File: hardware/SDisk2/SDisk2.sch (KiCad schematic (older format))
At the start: 34 parts

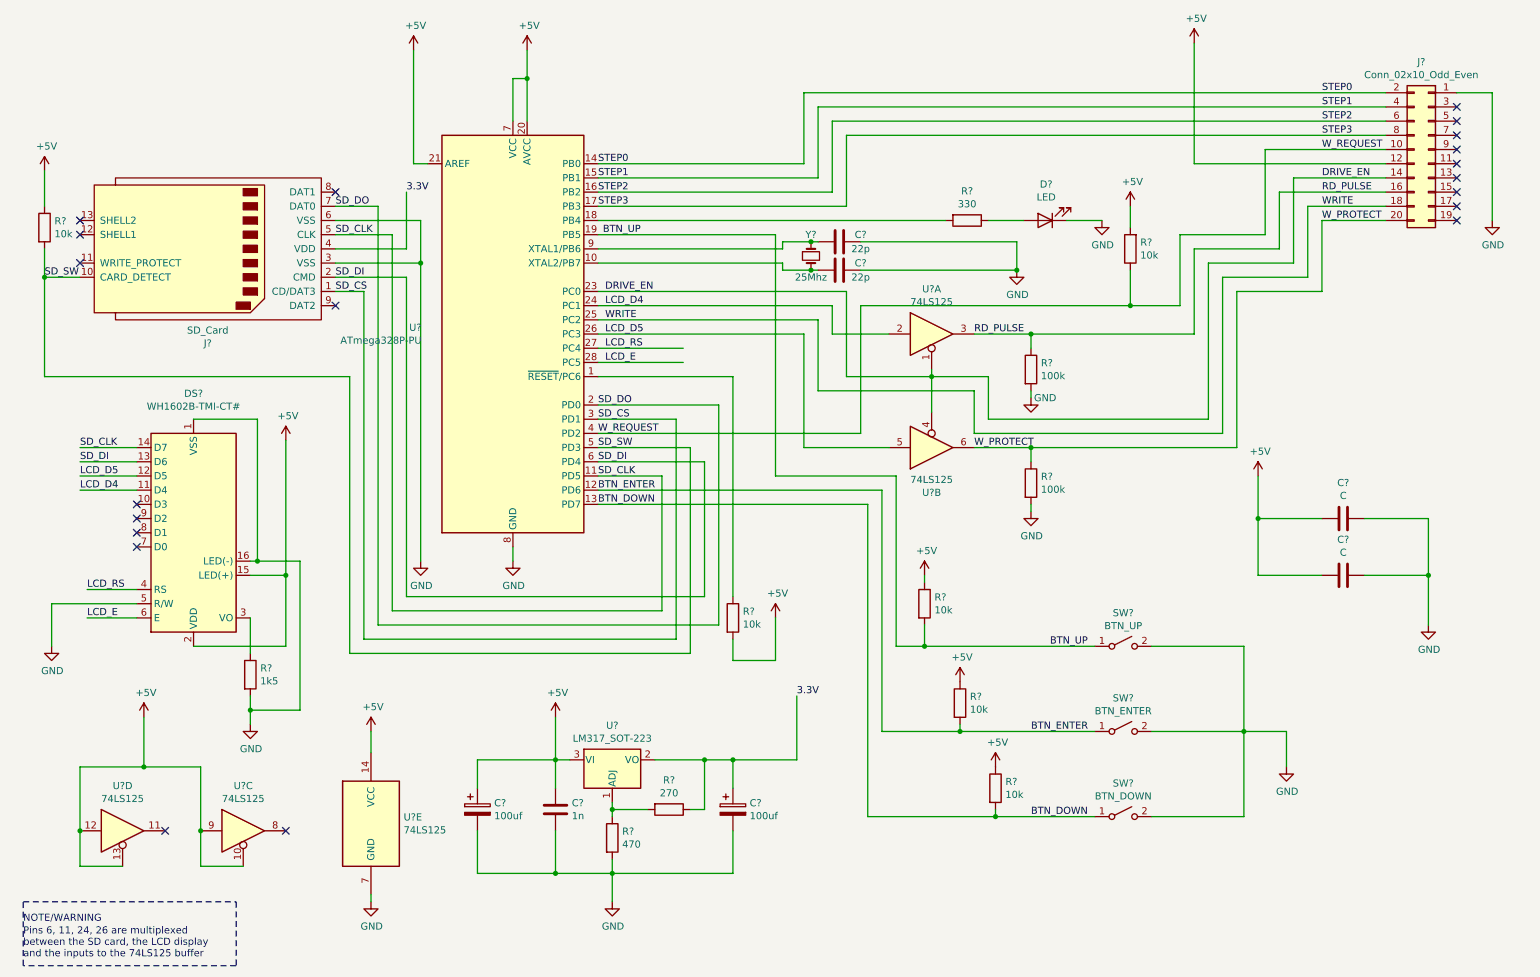
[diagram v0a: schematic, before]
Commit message: Associate footprints for most of the components
Need to create footprints for sdcard holder and LCD display

Signed-off-by: Rangel Ivanov <rangelivanov88@gmail.com>
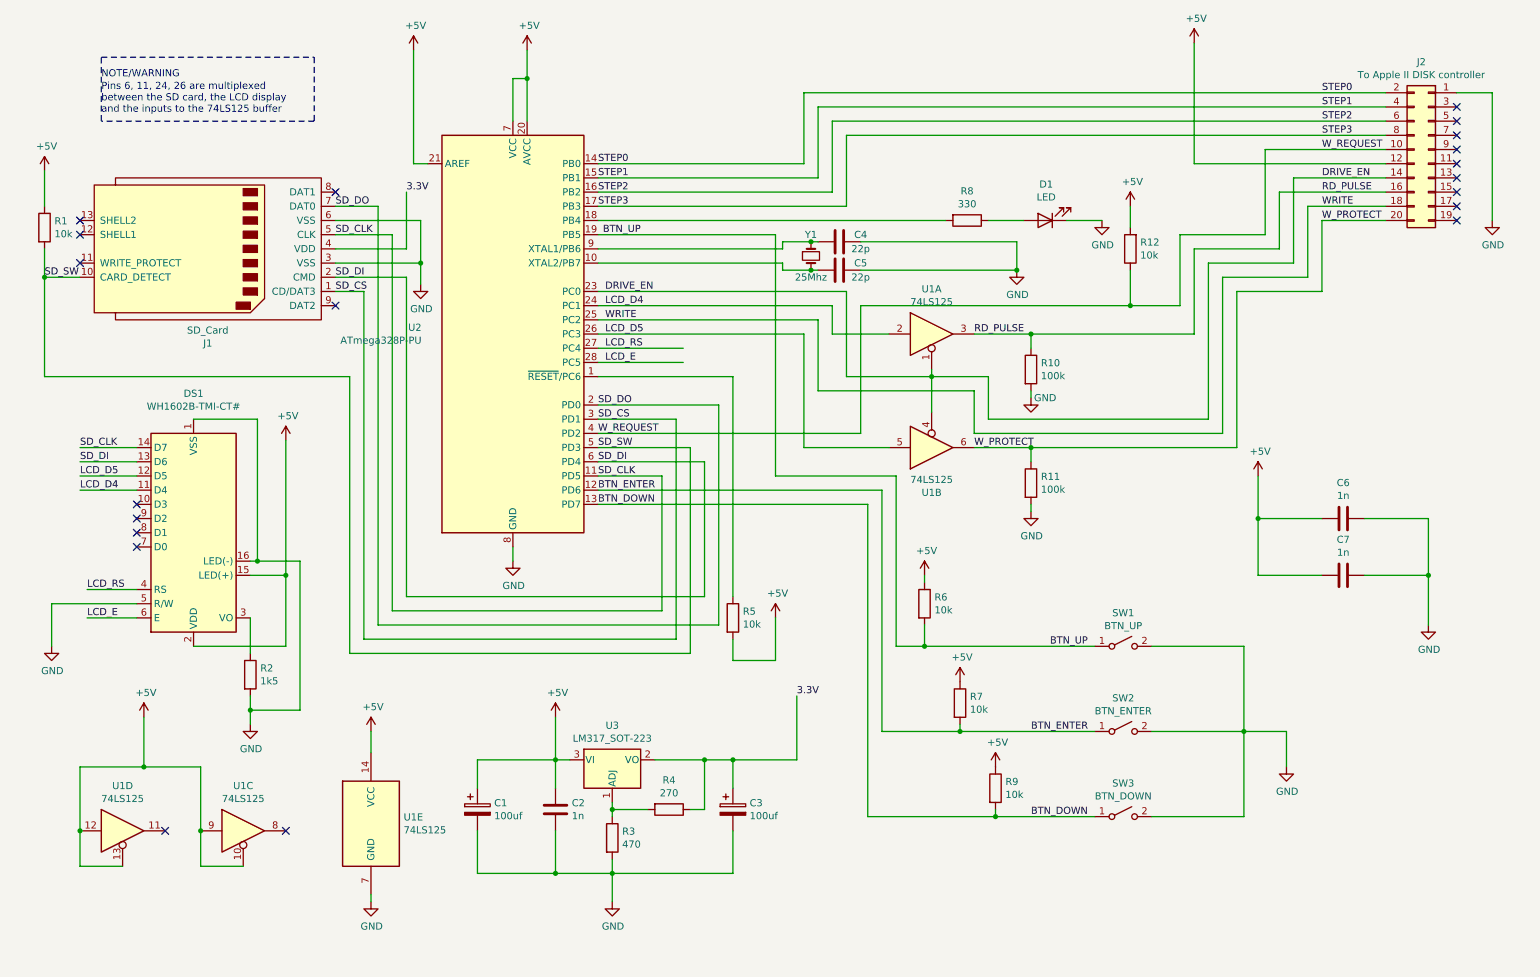
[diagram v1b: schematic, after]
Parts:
- C1, C3: renamed from C?; footprint (none) -> Capacitor_THT:CP_Radial_D5.0mm_P2.00mm
- C2, C4, C5: renamed from C?; footprint (none) -> Capacitor_THT:C_Disc_D3.0mm_W1.6mm_P2.50mm
- C6, C7: renamed from C?; value C -> 1n; footprint (none) -> Capacitor_THT:C_Disc_D3.0mm_W1.6mm_P2.50mm
- D1: renamed from D?; footprint (none) -> LED_THT:LED_D3.0mm
- DS1: renamed from DS?; footprint Display:WC1602A -> (none)
- J2: renamed from J?; value Conn_02x10_Odd_Even -> To Apple II DISK controller; footprint (none) -> Connector_PinHeader_2.54mm:PinHeader_2x10_P2.54mm_Horizontal
- R1, R10, R11, R12, R2, R3, R5, R6, R7, R8, R9: renamed from R?; footprint (none) -> Resistor_THT:R_Axial_DIN0204_L3.6mm_D1.6mm_P5.08mm_Horizontal
- R4: renamed from R?; footprint (none) -> Resistor_THT:R_Axial_DIN0204_L3.6mm_D1.6mm_P5.08mm_Vertical
- SW1, SW2, SW3: renamed from SW?; footprint (none) -> Button_Switch_THT:SW_PUSH_6mm
- U1: renamed from U?; footprint (none) -> Package_DIP:DIP-14_W7.62mm
- U3: renamed from U?; footprint Package_TO_SOT_SMD:SOT-223-3_TabPin2 -> Package_TO_SOT_THT:TO-220-3_Vertical
- Y1: renamed from Y?; footprint (none) -> Crystal:Crystal_HC49-4H_Vertical
- gave numbers to parts that had none: 2

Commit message: Add SDCard footprint and datasheet
Signed-off-by: Rangel Ivanov <rangelivanov88@gmail.com>
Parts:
- J1: footprint (none) -> SDisk2:attend-104d-tca0-r06-sdcard-holder; symbol Connector:SD_Card -> SDisk2:SD_Card
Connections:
- net GND: now also J1.13 (GND)
- no-connect marks 20 -> 19
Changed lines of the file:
@@
 	-1   0    0    1
 $EndComp
-Wire Wire Line
-	8350 2250 8350 2100
 $Comp
 L power:+5V #PWR0110
@@
 Wire Wire Line
 	2950 2700 2750 2700
-$Comp
-L Connector:SD_Card J1
-U 1 1 5FF919EB
-P 1850 2400
-F 0 "J1" H 1850 3065 50  0000 C CNN
-F 1 "SD_Card" H 1850 2974 50  0000 C CNN
-F 2 "" H 1850 2400 50  0001 C CNN
-F 3 "http://portal.fciconnect.com/Comergent//fci/drawing/10067847.pdf" H 1850 2400 50  0001 C CNN
-	1    1850 2400
-	-1   0    0    1
-$EndComp
 Text Label 2750 2100 0    50   ~ 0
 SD_DO
@@
 Text Notes 1100 1200 0    50   ~ 0
 NOTE/WARNING\n
-NoConn ~ 950  2200
 NoConn ~ 950  2300
 Text Label 7650 6400 0    50   ~ 0
@@
 Text Label 8050 5200 2    50   ~ 0
 BTN_UP
+Wire Wire Line
+	8350 2050 8350 2100
+Connection ~ 8350 2100
+Wire Wire Line
+	8350 2100 8350 2250
+$Comp
+L SDisk2:SD_Card J1
+U 1 1 5FF919EB
+P 1850 2400
+F 0 "J1" H 1850 3065 50  0000 C CNN
+F 1 "SD_Card" H 1850 2974 50  0000 C CNN
+F 2 "SDisk2:attend-104d-tca0-r06-sdcard-holder" H 1850 2400 50  0001 C CNN
+F 3 "http://portal.fciconnect.com/Comergent//fci/drawing/10067847.pdf" H 1850 2400 50  0001 C CNN
+	1    1850 2400
+	-1   0    0    1
+$EndComp
+Wire Wire Line
+	950  2200 900  2200
+Wire Wire Line
+	900  2200 900  2950
+$Comp
+L power:GND #PWR0128
+U 1 1 5FFFE7B3
+P 900 2950
+F 0 "#PWR0128" H 900 2700 50  0001 C CNN
+F 1 "GND" H 905 2777 50  0000 C CNN
+F 2 "" H 900 2950 50  0001 C CNN
+F 3 "" H 900 2950 50  0001 C CNN
+	1    900  2950
+	1    0    0    -1
+$EndComp
 $EndSCHEMATC

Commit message: Create netlist and begin place and route
Signed-off-by: Rangel Ivanov <rangelivanov88@gmail.com>
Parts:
- DS1: footprint (none) -> Connector_PinHeader_2.54mm:PinHeader_1x16_P2.54mm_Vertical
- R4: footprint Resistor_THT:R_Axial_DIN0204_L3.6mm_D1.6mm_P5.08mm_Vertical -> Resistor_THT:R_Axial_DIN0204_L3.6mm_D1.6mm_P5.08mm_Horizontal
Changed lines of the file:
@@
 F 0 "R4" V 4893 6350 50  0000 C CNN
 F 1 "270" V 4984 6350 50  0000 C CNN
-F 2 "Resistor_THT:R_Axial_DIN0204_L3.6mm_D1.6mm_P5.08mm_Vertical" V 5030 6350 50  0001 C CNN
+F 2 "Resistor_THT:R_Axial_DIN0204_L3.6mm_D1.6mm_P5.08mm_Horizontal" V 5030 6350 50  0001 C CNN
 F 3 "~" H 5100 6350 50  0001 C CNN
 	1    5100 6350
@@
 F 0 "DS1" H 1750 3419 50  0000 C CNN
 F 1 "WH1602B-TMI-CT# " H 1750 3510 50  0000 C CNN
-F 2 "" H 1750 3500 50  0001 C CIN
+F 2 "Connector_PinHeader_2.54mm:PinHeader_1x16_P2.54mm_Vertical" H 1750 3500 50  0001 C CIN
 F 3 "https://store.comet.bg/download-file.php?id=1596" H 2450 4400 50  0001 C CNN
 	1    1750 4400
@@
 F 1 "SD_Card" H 1850 2974 50  0000 C CNN
 F 2 "SDisk2:attend-104d-tca0-r06-sdcard-holder" H 1850 2400 50  0001 C CNN
-F 3 "http://portal.fciconnect.com/Comergent//fci/drawing/10067847.pdf" H 1850 2400 50  0001 C CNN
+F 3 "https://store.comet.bg/download-file.php?id=8828" H 1850 2400 50  0001 C CNN
 	1    1850 2400
 	-1   0    0    1

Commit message: Move symbols to project specific symbol library
Signed-off-by: Rangel Ivanov <rangelivanov88@gmail.com>
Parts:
- DS1: symbol Display_Character:WC1602A -> SDisk2:WC1602B
- U1: symbol 74xx:74LS125 -> SDisk2:74LS125
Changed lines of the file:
@@
 $EndComp
 $Comp
-L 74xx:74LS125 U1
+L SDisk2:74LS125 U1
 U 2 1 5FF8AA8E
 P 6950 3800
@@
 $EndComp
 $Comp
-L 74xx:74LS125 U1
+L SDisk2:74LS125 U1
 U 3 1 5FF8B384
 P 2100 6500
@@
 $EndComp
 $Comp
-L 74xx:74LS125 U1
+L SDisk2:74LS125 U1
 U 5 1 5FF8C405
 P 3000 6450
@@
 	950  6500 950  6750
 $Comp
-L 74xx:74LS125 U1
+L SDisk2:74LS125 U1
 U 4 1 5FF8B9E8
 P 1250 6500
@@
 $EndComp
 $Comp
-L 74xx:74LS125 U1
+L SDisk2:74LS125 U1
 U 1 1 5FF89C47
 P 6950 3000
@@
 NoConn ~ 1350 4500
 $Comp
-L Display_Character:WC1602A DS1
+L SDisk2:WC1602B DS1
 U 1 1 6085C96E
 P 1750 4400

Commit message: Move all symbols into the SDisk2 project specific library
Signed-off-by: Rangel Ivanov <rangelivanov88@gmail.com>
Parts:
- C1, C3: symbol Device:CP -> SDisk2:CP-Device
- C2, C4, C5, C6, C7: symbol Device:C -> SDisk2:C-Device
- D1: symbol Device:LED -> SDisk2:LED-Device
- J2: symbol Connector_Generic:Conn_02x10_Odd_Even -> SDisk2:Conn_02x10_Odd_Even-Connector_Generic
- R1, R10, R11, R12, R2, R3, R4, R5, R6, R7, R8, R9: symbol Device:R -> SDisk2:R-Device
- SW1, SW2, SW3: symbol Switch:SW_SPST -> SDisk2:SW_SPST-Switch
- U2: symbol MCU_Microchip_ATmega:ATmega328P-PU -> SDisk2:ATmega328P-PU-MCU_Microchip_ATmega
- U3: symbol Regulator_Linear:LM317_SOT-223 -> SDisk2:LM317_SOT-223-Regulator_Linear
- Y1: symbol Device:Crystal_Small -> SDisk2:Crystal_Small-Device
